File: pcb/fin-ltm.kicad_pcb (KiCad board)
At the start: 2 copper layers, 121 parts, among them J1 Connector, USB-TYPE-C-16P, Q1 MMBT3904, Q2 HL3415A, U1 ESP32-C3FH4, U2 RT9080, U3 SN74LV1T34DBV, X1 40MHz, 15pF

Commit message: server updates and battling with kicad
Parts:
- removed D11, D12, D13, D14, D15, D16, D17, D18, D19, D20, D21, D22, D23, D24, D25, D26, D27, D28, D29, D30, D31, D32, D33, D34, D35, D36, D37, D38, D39, D40, D41, D42, D43, D44, D45, D46, D47, D48, D49, D50, D51, D52, D53, D54, D55, D56, D57, D58, D59, D60, D61, D62, D63, D64, D65: WS2812B, PCM_JLCPCB:LED-SMD_4P-L1.6-W1.5_XL-1615RGBC-WS2812B
- added D101: WS2812B, PCM_JLCPCB:LED-SMD_4P-L1.6-W1.5_XL-1615RGBC-WS2812B, F.Cu at (66.6, 17.8)
- added D102: WS2812B, PCM_JLCPCB:LED-SMD_4P-L1.6-W1.5_XL-1615RGBC-WS2812B, F.Cu at (66.6, 20.4)
- added D103: WS2812B, PCM_JLCPCB:LED-SMD_4P-L1.6-W1.5_XL-1615RGBC-WS2812B, F.Cu at (66.6, 23.1)
- added D104: WS2812B, PCM_JLCPCB:LED-SMD_4P-L1.6-W1.5_XL-1615RGBC-WS2812B, F.Cu at (66.6, 25.7)
- added D105: WS2812B, PCM_JLCPCB:LED-SMD_4P-L1.6-W1.5_XL-1615RGBC-WS2812B, F.Cu at (66.6, 28.4)
- added D106: WS2812B, PCM_JLCPCB:LED-SMD_4P-L1.6-W1.5_XL-1615RGBC-WS2812B, F.Cu at (66.6, 31.0)
- added D107: WS2812B, PCM_JLCPCB:LED-SMD_4P-L1.6-W1.5_XL-1615RGBC-WS2812B, F.Cu at (66.6, 33.6)
- added D108: WS2812B, PCM_JLCPCB:LED-SMD_4P-L1.6-W1.5_XL-1615RGBC-WS2812B, F.Cu at (66.6, 36.3)
- added D109: WS2812B, PCM_JLCPCB:LED-SMD_4P-L1.6-W1.5_XL-1615RGBC-WS2812B, F.Cu at (66.6, 39.0)
- added D110: WS2812B, PCM_JLCPCB:LED-SMD_4P-L1.6-W1.5_XL-1615RGBC-WS2812B, F.Cu at (66.6, 41.6)
- added D111: WS2812B, PCM_JLCPCB:LED-SMD_4P-L1.6-W1.5_XL-1615RGBC-WS2812B, F.Cu at (66.6, 44.2)
- added D112: WS2812B, PCM_JLCPCB:LED-SMD_4P-L1.6-W1.5_XL-1615RGBC-WS2812B, F.Cu at (66.6, 46.9)
- added D113: WS2812B, PCM_JLCPCB:LED-SMD_4P-L1.6-W1.5_XL-1615RGBC-WS2812B, F.Cu at (66.6, 49.5)
- added D114: WS2812B, PCM_JLCPCB:LED-SMD_4P-L1.6-W1.5_XL-1615RGBC-WS2812B, F.Cu at (70.0, 17.8)
- added D115: WS2812B, PCM_JLCPCB:LED-SMD_4P-L1.6-W1.5_XL-1615RGBC-WS2812B, F.Cu at (70.0, 20.4)
- added D116: WS2812B, PCM_JLCPCB:LED-SMD_4P-L1.6-W1.5_XL-1615RGBC-WS2812B, F.Cu at (70.0, 23.1)
- added D117: WS2812B, PCM_JLCPCB:LED-SMD_4P-L1.6-W1.5_XL-1615RGBC-WS2812B, F.Cu at (70.0, 25.7)
- added D118: WS2812B, PCM_JLCPCB:LED-SMD_4P-L1.6-W1.5_XL-1615RGBC-WS2812B, F.Cu at (70.0, 28.4)
- added D119: WS2812B, PCM_JLCPCB:LED-SMD_4P-L1.6-W1.5_XL-1615RGBC-WS2812B, F.Cu at (70.0, 31.0)
- added D120: WS2812B, PCM_JLCPCB:LED-SMD_4P-L1.6-W1.5_XL-1615RGBC-WS2812B, F.Cu at (70.0, 33.6)
- added D121: WS2812B, PCM_JLCPCB:LED-SMD_4P-L1.6-W1.5_XL-1615RGBC-WS2812B, F.Cu at (70.0, 36.3)
- added D122: WS2812B, PCM_JLCPCB:LED-SMD_4P-L1.6-W1.5_XL-1615RGBC-WS2812B, F.Cu at (70.0, 39.0)
- added D123: WS2812B, PCM_JLCPCB:LED-SMD_4P-L1.6-W1.5_XL-1615RGBC-WS2812B, F.Cu at (70.0, 41.6)
- added D124: WS2812B, PCM_JLCPCB:LED-SMD_4P-L1.6-W1.5_XL-1615RGBC-WS2812B, F.Cu at (70.0, 44.2)
- added D125: WS2812B, PCM_JLCPCB:LED-SMD_4P-L1.6-W1.5_XL-1615RGBC-WS2812B, F.Cu at (70.0, 46.9)
- added D126: WS2812B, PCM_JLCPCB:LED-SMD_4P-L1.6-W1.5_XL-1615RGBC-WS2812B, F.Cu at (70.0, 49.5)
- added D127: WS2812B, PCM_JLCPCB:LED-SMD_4P-L1.6-W1.5_XL-1615RGBC-WS2812B, F.Cu at (73.5, 17.8)
- added D128: WS2812B, PCM_JLCPCB:LED-SMD_4P-L1.6-W1.5_XL-1615RGBC-WS2812B, F.Cu at (73.5, 20.4)
- added D129: WS2812B, PCM_JLCPCB:LED-SMD_4P-L1.6-W1.5_XL-1615RGBC-WS2812B, F.Cu at (73.5, 23.1)
- added D130: WS2812B, PCM_JLCPCB:LED-SMD_4P-L1.6-W1.5_XL-1615RGBC-WS2812B, F.Cu at (73.5, 25.7)
- added D131: WS2812B, PCM_JLCPCB:LED-SMD_4P-L1.6-W1.5_XL-1615RGBC-WS2812B, F.Cu at (73.5, 28.4)
- added D132: WS2812B, PCM_JLCPCB:LED-SMD_4P-L1.6-W1.5_XL-1615RGBC-WS2812B, F.Cu at (73.5, 31.0)
- added D133: WS2812B, PCM_JLCPCB:LED-SMD_4P-L1.6-W1.5_XL-1615RGBC-WS2812B, F.Cu at (73.5, 33.6)
- added D134: WS2812B, PCM_JLCPCB:LED-SMD_4P-L1.6-W1.5_XL-1615RGBC-WS2812B, F.Cu at (73.5, 36.3)
- added D135: WS2812B, PCM_JLCPCB:LED-SMD_4P-L1.6-W1.5_XL-1615RGBC-WS2812B, F.Cu at (73.5, 39.0)
- added D136: WS2812B, PCM_JLCPCB:LED-SMD_4P-L1.6-W1.5_XL-1615RGBC-WS2812B, F.Cu at (73.5, 41.6)
- added D137: WS2812B, PCM_JLCPCB:LED-SMD_4P-L1.6-W1.5_XL-1615RGBC-WS2812B, F.Cu at (73.5, 44.2)
- added D138: WS2812B, PCM_JLCPCB:LED-SMD_4P-L1.6-W1.5_XL-1615RGBC-WS2812B, F.Cu at (73.5, 46.9)
- added D139: WS2812B, PCM_JLCPCB:LED-SMD_4P-L1.6-W1.5_XL-1615RGBC-WS2812B, F.Cu at (73.5, 49.5)
- added D140: WS2812B, PCM_JLCPCB:LED-SMD_4P-L1.6-W1.5_XL-1615RGBC-WS2812B, F.Cu at (77.0, 17.8)
- added D141: WS2812B, PCM_JLCPCB:LED-SMD_4P-L1.6-W1.5_XL-1615RGBC-WS2812B, F.Cu at (77.0, 20.4)
- added D142: WS2812B, PCM_JLCPCB:LED-SMD_4P-L1.6-W1.5_XL-1615RGBC-WS2812B, F.Cu at (77.0, 23.1)
- added D143: WS2812B, PCM_JLCPCB:LED-SMD_4P-L1.6-W1.5_XL-1615RGBC-WS2812B, F.Cu at (77.0, 25.7)
- added D144: WS2812B, PCM_JLCPCB:LED-SMD_4P-L1.6-W1.5_XL-1615RGBC-WS2812B, F.Cu at (77.0, 28.4)
- added D145: WS2812B, PCM_JLCPCB:LED-SMD_4P-L1.6-W1.5_XL-1615RGBC-WS2812B, F.Cu at (77.0, 31.0)
- added D146: WS2812B, PCM_JLCPCB:LED-SMD_4P-L1.6-W1.5_XL-1615RGBC-WS2812B, F.Cu at (77.0, 33.6)
- added D147: WS2812B, PCM_JLCPCB:LED-SMD_4P-L1.6-W1.5_XL-1615RGBC-WS2812B, F.Cu at (77.0, 36.3)
- added D148: WS2812B, PCM_JLCPCB:LED-SMD_4P-L1.6-W1.5_XL-1615RGBC-WS2812B, F.Cu at (77.0, 39.0)
- added D149: WS2812B, PCM_JLCPCB:LED-SMD_4P-L1.6-W1.5_XL-1615RGBC-WS2812B, F.Cu at (77.0, 41.6)
- added D150: WS2812B, PCM_JLCPCB:LED-SMD_4P-L1.6-W1.5_XL-1615RGBC-WS2812B, F.Cu at (77.0, 44.2)
- added D151: WS2812B, PCM_JLCPCB:LED-SMD_4P-L1.6-W1.5_XL-1615RGBC-WS2812B, F.Cu at (77.0, 46.9)
- added D152: WS2812B, PCM_JLCPCB:LED-SMD_4P-L1.6-W1.5_XL-1615RGBC-WS2812B, F.Cu at (77.0, 49.5)
- added D153: WS2812B, PCM_JLCPCB:LED-SMD_4P-L1.6-W1.5_XL-1615RGBC-WS2812B, F.Cu at (80.4, 17.8)
- added D154: WS2812B, PCM_JLCPCB:LED-SMD_4P-L1.6-W1.5_XL-1615RGBC-WS2812B, F.Cu at (80.4, 20.4)
- added D155: WS2812B, PCM_JLCPCB:LED-SMD_4P-L1.6-W1.5_XL-1615RGBC-WS2812B, F.Cu at (80.4, 23.1)
- added D156: WS2812B, PCM_JLCPCB:LED-SMD_4P-L1.6-W1.5_XL-1615RGBC-WS2812B, F.Cu at (80.4, 25.7)
- added D157: WS2812B, PCM_JLCPCB:LED-SMD_4P-L1.6-W1.5_XL-1615RGBC-WS2812B, F.Cu at (80.4, 28.4)
- added D158: WS2812B, PCM_JLCPCB:LED-SMD_4P-L1.6-W1.5_XL-1615RGBC-WS2812B, F.Cu at (80.4, 31.0)
- added D159: WS2812B, PCM_JLCPCB:LED-SMD_4P-L1.6-W1.5_XL-1615RGBC-WS2812B, F.Cu at (80.4, 33.6)
- added D160: WS2812B, PCM_JLCPCB:LED-SMD_4P-L1.6-W1.5_XL-1615RGBC-WS2812B, F.Cu at (80.4, 36.3)
- added D161: WS2812B, PCM_JLCPCB:LED-SMD_4P-L1.6-W1.5_XL-1615RGBC-WS2812B, F.Cu at (80.4, 39.0)
- added D162: WS2812B, PCM_JLCPCB:LED-SMD_4P-L1.6-W1.5_XL-1615RGBC-WS2812B, F.Cu at (80.4, 41.6)
- added D163: WS2812B, PCM_JLCPCB:LED-SMD_4P-L1.6-W1.5_XL-1615RGBC-WS2812B, F.Cu at (80.4, 44.2)
- added D164: WS2812B, PCM_JLCPCB:LED-SMD_4P-L1.6-W1.5_XL-1615RGBC-WS2812B, F.Cu at (80.4, 46.9)
- added D165: WS2812B, PCM_JLCPCB:LED-SMD_4P-L1.6-W1.5_XL-1615RGBC-WS2812B, F.Cu at (80.4, 49.5)
- added D166: WS2812B, PCM_JLCPCB:LED-SMD_4P-L1.6-W1.5_XL-1615RGBC-WS2812B, F.Cu at (83.8, 17.8)
- added D167: WS2812B, PCM_JLCPCB:LED-SMD_4P-L1.6-W1.5_XL-1615RGBC-WS2812B, F.Cu at (83.8, 20.4)
- added D168: WS2812B, PCM_JLCPCB:LED-SMD_4P-L1.6-W1.5_XL-1615RGBC-WS2812B, F.Cu at (83.8, 23.1)
- added D169: WS2812B, PCM_JLCPCB:LED-SMD_4P-L1.6-W1.5_XL-1615RGBC-WS2812B, F.Cu at (83.8, 25.7)
- added D170: WS2812B, PCM_JLCPCB:LED-SMD_4P-L1.6-W1.5_XL-1615RGBC-WS2812B, F.Cu at (83.8, 28.4)
- added D171: WS2812B, PCM_JLCPCB:LED-SMD_4P-L1.6-W1.5_XL-1615RGBC-WS2812B, F.Cu at (83.8, 31.0)
- added D172: WS2812B, PCM_JLCPCB:LED-SMD_4P-L1.6-W1.5_XL-1615RGBC-WS2812B, F.Cu at (83.8, 33.6)
- added D173: WS2812B, PCM_JLCPCB:LED-SMD_4P-L1.6-W1.5_XL-1615RGBC-WS2812B, F.Cu at (83.8, 36.3)
- added D174: WS2812B, PCM_JLCPCB:LED-SMD_4P-L1.6-W1.5_XL-1615RGBC-WS2812B, F.Cu at (83.8, 39.0)
- added D175: WS2812B, PCM_JLCPCB:LED-SMD_4P-L1.6-W1.5_XL-1615RGBC-WS2812B, F.Cu at (83.8, 41.6)
- added D176: WS2812B, PCM_JLCPCB:LED-SMD_4P-L1.6-W1.5_XL-1615RGBC-WS2812B, F.Cu at (83.8, 44.2)
- added D177: WS2812B, PCM_JLCPCB:LED-SMD_4P-L1.6-W1.5_XL-1615RGBC-WS2812B, F.Cu at (83.8, 46.9)
- added D178: WS2812B, PCM_JLCPCB:LED-SMD_4P-L1.6-W1.5_XL-1615RGBC-WS2812B, F.Cu at (83.8, 49.5)
- added D179: WS2812B, PCM_JLCPCB:LED-SMD_4P-L1.6-W1.5_XL-1615RGBC-WS2812B, F.Cu at (87.3, 17.8)
- added D180: WS2812B, PCM_JLCPCB:LED-SMD_4P-L1.6-W1.5_XL-1615RGBC-WS2812B, F.Cu at (87.3, 20.4)
- added D181: WS2812B, PCM_JLCPCB:LED-SMD_4P-L1.6-W1.5_XL-1615RGBC-WS2812B, F.Cu at (87.3, 23.1)
- added D182: WS2812B, PCM_JLCPCB:LED-SMD_4P-L1.6-W1.5_XL-1615RGBC-WS2812B, F.Cu at (87.3, 25.7)
- added D183: WS2812B, PCM_JLCPCB:LED-SMD_4P-L1.6-W1.5_XL-1615RGBC-WS2812B, F.Cu at (87.3, 28.4)
- added D184: WS2812B, PCM_JLCPCB:LED-SMD_4P-L1.6-W1.5_XL-1615RGBC-WS2812B, F.Cu at (87.3, 31.0)
- added D185: WS2812B, PCM_JLCPCB:LED-SMD_4P-L1.6-W1.5_XL-1615RGBC-WS2812B, F.Cu at (87.3, 33.6)
- added D186: WS2812B, PCM_JLCPCB:LED-SMD_4P-L1.6-W1.5_XL-1615RGBC-WS2812B, F.Cu at (87.3, 36.3)
- added D187: WS2812B, PCM_JLCPCB:LED-SMD_4P-L1.6-W1.5_XL-1615RGBC-WS2812B, F.Cu at (87.3, 39.0)
- added D188: WS2812B, PCM_JLCPCB:LED-SMD_4P-L1.6-W1.5_XL-1615RGBC-WS2812B, F.Cu at (87.3, 41.6)
- added D189: WS2812B, PCM_JLCPCB:LED-SMD_4P-L1.6-W1.5_XL-1615RGBC-WS2812B, F.Cu at (87.3, 44.2)
- added D190: WS2812B, PCM_JLCPCB:LED-SMD_4P-L1.6-W1.5_XL-1615RGBC-WS2812B, F.Cu at (87.3, 46.9)
- added D191: WS2812B, PCM_JLCPCB:LED-SMD_4P-L1.6-W1.5_XL-1615RGBC-WS2812B, F.Cu at (87.3, 49.5)
- added D192: WS2812B, PCM_JLCPCB:LED-SMD_4P-L1.6-W1.5_XL-1615RGBC-WS2812B, F.Cu at (90.8, 17.8)
- added D193: WS2812B, PCM_JLCPCB:LED-SMD_4P-L1.6-W1.5_XL-1615RGBC-WS2812B, F.Cu at (90.8, 20.4)
- added D194: WS2812B, PCM_JLCPCB:LED-SMD_4P-L1.6-W1.5_XL-1615RGBC-WS2812B, F.Cu at (90.8, 23.1)
- added D195: WS2812B, PCM_JLCPCB:LED-SMD_4P-L1.6-W1.5_XL-1615RGBC-WS2812B, F.Cu at (90.8, 25.7)
- added D196: WS2812B, PCM_JLCPCB:LED-SMD_4P-L1.6-W1.5_XL-1615RGBC-WS2812B, F.Cu at (90.8, 28.4)
- added D197: WS2812B, PCM_JLCPCB:LED-SMD_4P-L1.6-W1.5_XL-1615RGBC-WS2812B, F.Cu at (90.8, 31.0)
- added D198: WS2812B, PCM_JLCPCB:LED-SMD_4P-L1.6-W1.5_XL-1615RGBC-WS2812B, F.Cu at (90.8, 33.6)
- added D199: WS2812B, PCM_JLCPCB:LED-SMD_4P-L1.6-W1.5_XL-1615RGBC-WS2812B, F.Cu at (90.8, 36.3)
- added D200: WS2812B, PCM_JLCPCB:LED-SMD_4P-L1.6-W1.5_XL-1615RGBC-WS2812B, F.Cu at (90.8, 39.0)
- moved J1 58.5 mm to (54.8, 29.1)
- moved F1 23.5 mm to (57.2, 46.6)
- moved X1 23.5 mm to (51.9, 47.1)
- moved D6 23.5 mm to (61.1, 45.8)
- moved Q1 20.6 mm to (33.0, 44.5)
- moved Q2 20.6 mm to (33.0, 49.1)
- moved U2 20.1 mm to (57.7, 37.3)
- moved U3 20.1 mm to (57.7, 41.9)
- moved U1 19.0 mm to (38.9, 45.6)
- moved C10 18.5 mm to (47.1, 51.5)
- moved C8 18.5 mm to (47.1, 45.4)
- moved C9 18.5 mm to (47.1, 48.4)
- moved D10 18.5 mm to (47.1, 42.3)
- moved D7 18.5 mm to (47.1, 33.1)
- moved D8 18.5 mm to (47.1, 36.2)
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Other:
- board text removed: "REF**"

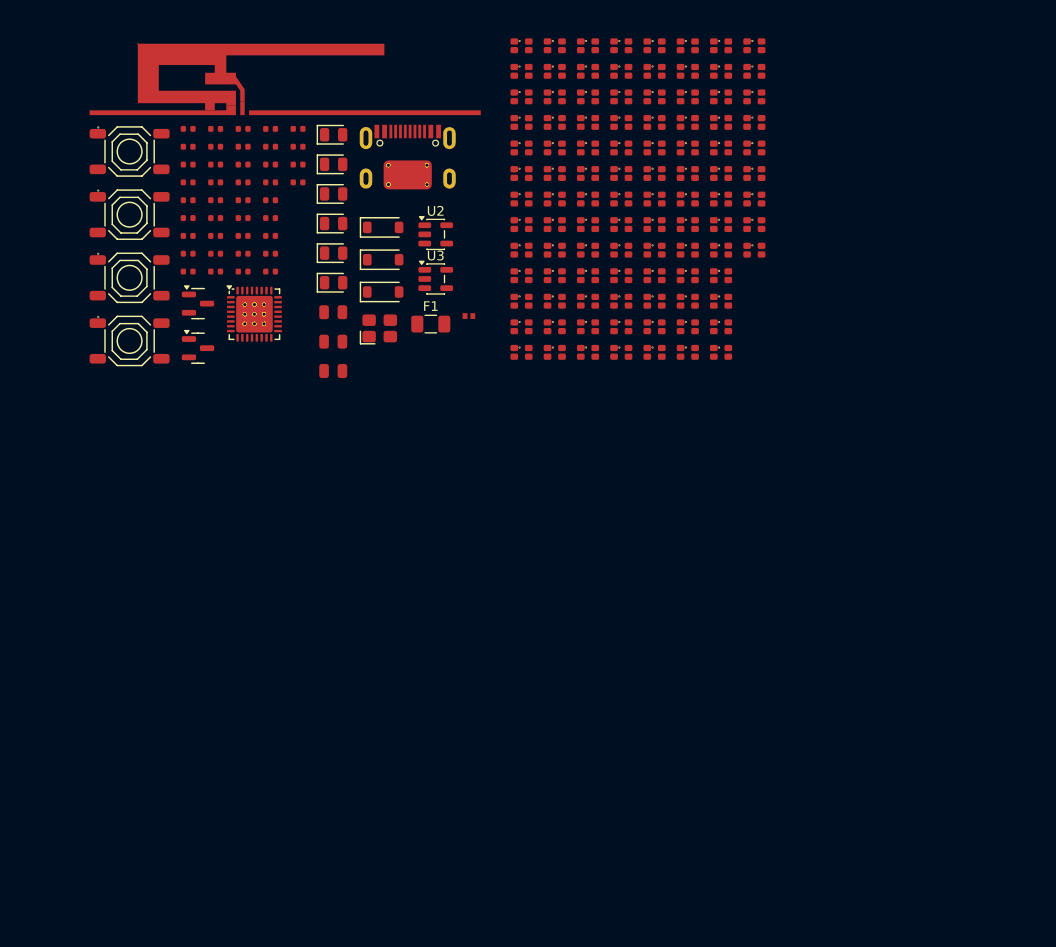
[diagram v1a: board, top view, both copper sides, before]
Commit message: pcb designed antenna
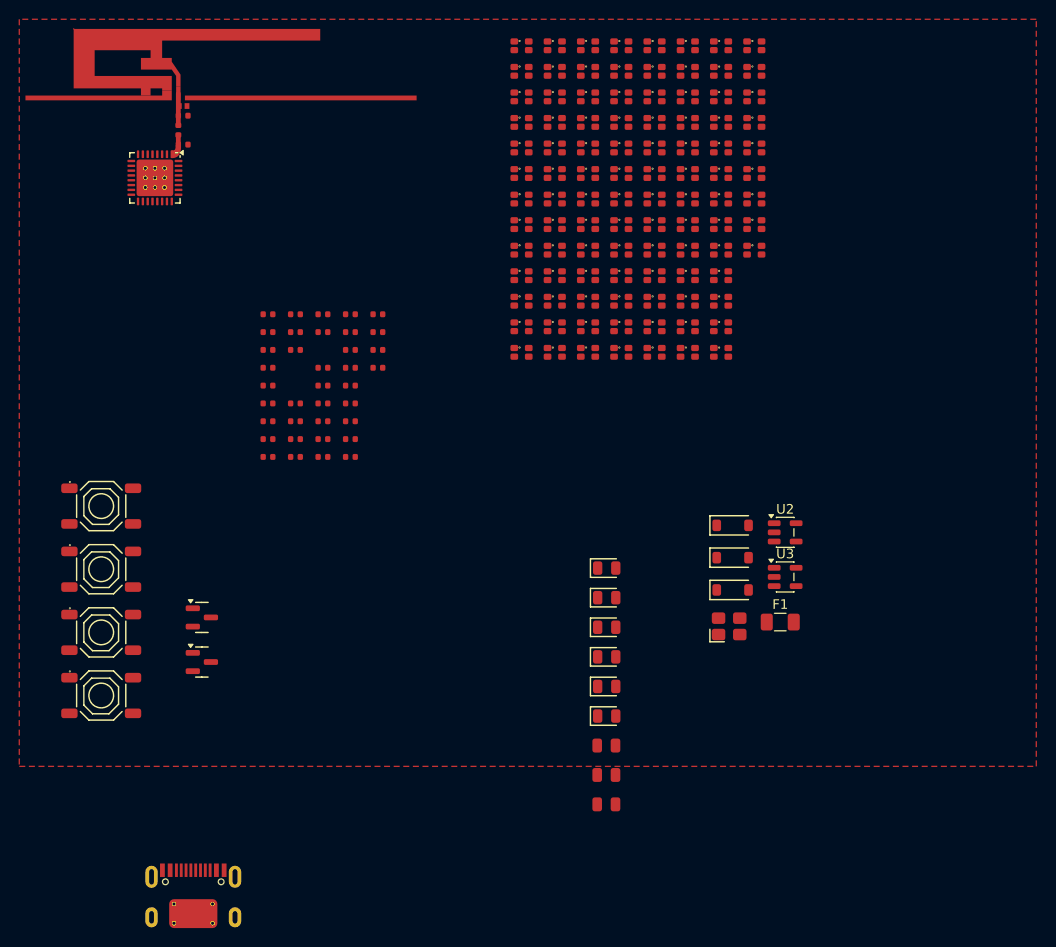
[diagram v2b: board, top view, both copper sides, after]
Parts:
- moved J1 79.8 mm to (32.5, 105.8)
- moved C8 53.1 mm to (75.4, 90.3)
- moved C9 53.1 mm to (75.4, 93.4)
- moved C10 53.1 mm to (75.4, 96.4)
- moved D7 53.1 mm to (75.4, 78.1)
- moved D9 53.1 mm to (75.4, 84.2)
- moved D1 53.1 mm to (75.4, 71.9)
- moved D10 53.1 mm to (75.4, 87.3)
- moved D5 53.1 mm to (75.4, 75.0)
- moved D8 53.1 mm to (75.4, 81.1)
- moved D4 47.6 mm to (88.5, 74.2)
- moved F1 47.6 mm to (93.4, 77.5)
- moved D2 47.6 mm to (88.5, 67.5)
- moved D3 47.6 mm to (88.5, 70.8)
- moved U2 47.6 mm to (94.0, 68.2)
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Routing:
- net Net-(AE1-A): track 0.00 -> 3.30 mm
- net /Antenna: track 0.00 -> 1.00 mm
- added copper zone on F.Cu, net GND
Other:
- rule pad_to_mask_clearance: 0 -> 0.05

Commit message: pcb update and planning in svg
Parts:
- moved U3 83.6 mm to (20.6, 32.8), turned to 180 degrees
- moved X1 70.1 mm to (35.2, 32.0), turned to -90 degrees
- moved R9 36.2 mm to (16.9, 32.2), turned to 90 degrees
- moved R19 35.1 mm to (26.5, 26.8), turned to -90 degrees
- moved R8 34.5 mm to (17.9, 32.2), turned to 90 degrees
- moved R10 32.4 mm to (27.5, 26.8), turned to -90 degrees
- moved R18 32.4 mm to (28.5, 26.8), turned to -90 degrees
- moved C7 31.8 mm to (29.5, 26.8), turned to -90 degrees
- moved C6 29.6 mm to (24.2, 30.0)
- moved C11 26.2 mm to (27.8, 35.5), turned to -90 degrees
- moved C4 22.8 mm to (32.5, 29.8), turned to 180 degrees
- moved C5 22.1 mm to (26.8, 35.5), turned to 90 degrees
- moved L1 21.5 mm to (32.5, 30.8), turned to 180 degrees
- moved C15 19.8 mm to (33.0, 32.2), turned to 90 degrees
- moved C14 19.8 mm to (34.8, 29.5)
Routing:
- net /Leds/LED_DATA_5V: track 0.00 -> 27.1 mm, vias 0 -> 1
- net +3V3: track 0.00 -> 23.7 mm, vias 0 -> 4
- net Net-(U1-XTAL_N): track 0.00 -> 5.87 mm
- net /LED_DATA_3V3: track 0.00 -> 3.42 mm
- net Net-(C14-Pad1): track 0.00 -> 2.71 mm
- net /MODE_BUTTON: track 0.00 -> 2.03 mm
- net /POWER_BUTTON: track 0.00 -> 1.88 mm
- net /Reset: track 0.00 -> 1.82 mm
- net Net-(U3-Y): track 0.00 -> 1.63 mm
- net Net-(U1-(OUTPUT)_VDD_SPI): track 0.00 -> 1.28 mm
- net Net-(U1-XTAL_P): track 0.00 -> 1.00 mm
- net GND: vias 0 -> 20
- added copper zone on B.Cu, net GND
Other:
- board text added: "To led chain"

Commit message: more pcb routing
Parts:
- added J2: Test Connector, Library:Test_connector, F.Cu at (24.5, 52.3)
- moved S1 55.4 mm to (76.5, 79.9)
- moved S2 55.4 mm to (76.5, 86.5)
- moved S3 55.4 mm to (76.5, 93.0)
- moved S4 55.4 mm to (76.5, 99.5)
- moved J1 24.6 mm to (23.2, 83.0), turned to -90 degrees
- moved R11 18.5 mm to (43.8, 35.2), turned to 90 degrees
- moved C15 15.2 mm to (47.8, 36.0)
- moved U1 10.7 mm to (39.1, 33.7)
- moved C1 10.7 mm to (50.8, 47.9)
- moved C10 10.7 mm to (85.9, 98.7)
- moved C11 10.7 mm to (38.2, 37.8)
- moved C12 10.7 mm to (50.8, 62.6)
- moved C13 10.7 mm to (53.6, 47.9)
- moved C14 10.7 mm to (45.2, 31.8)
- moved C16 10.7 mm to (42.0, 27.2)
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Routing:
- net /USB_D+: track 0.00 -> 65.4 mm, vias 0 -> 2
- net /USB_D-: track 0.00 -> 64.4 mm, vias 0 -> 2
- net /Reset: track 1.82 -> 32.2 mm, vias 0 -> 1
- net /MCU_RX: track 0.00 -> 29.6 mm, vias 0 -> 1
- net /MCU_TX: track 0.00 -> 29.1 mm, vias 0 -> 1
- net /Leds/LED_DATA_5V: track 27.1 -> 6.18 mm
- net Net-(U1-U0TXD): track 0.00 -> 2.56 mm
- net Net-(U1-XTAL_N): track 5.87 -> 7.08 mm
- net /LED_DATA_3V3: track 3.42 -> 4.56 mm
- net GND: vias 20 -> 18
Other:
- board outline added: 112.5 x 77.3 mm

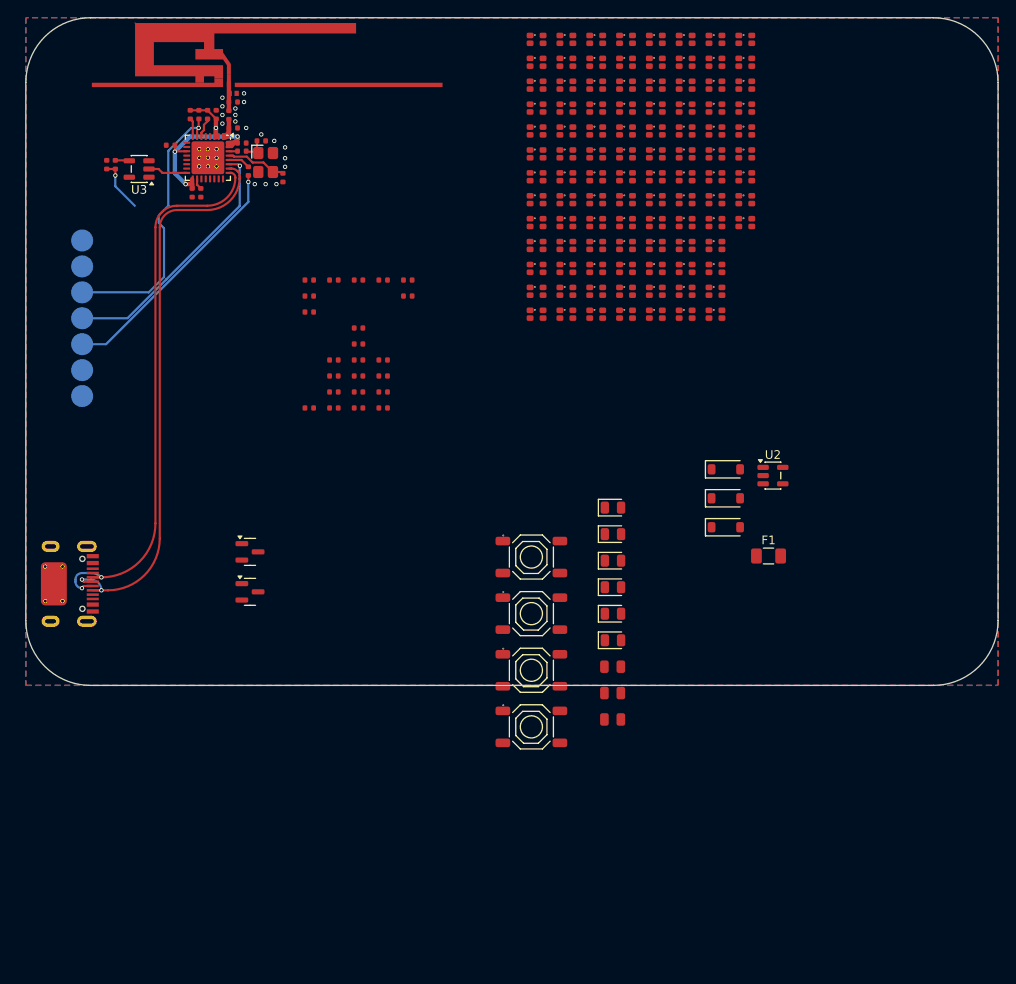
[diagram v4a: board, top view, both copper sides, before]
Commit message: even more pcb routing
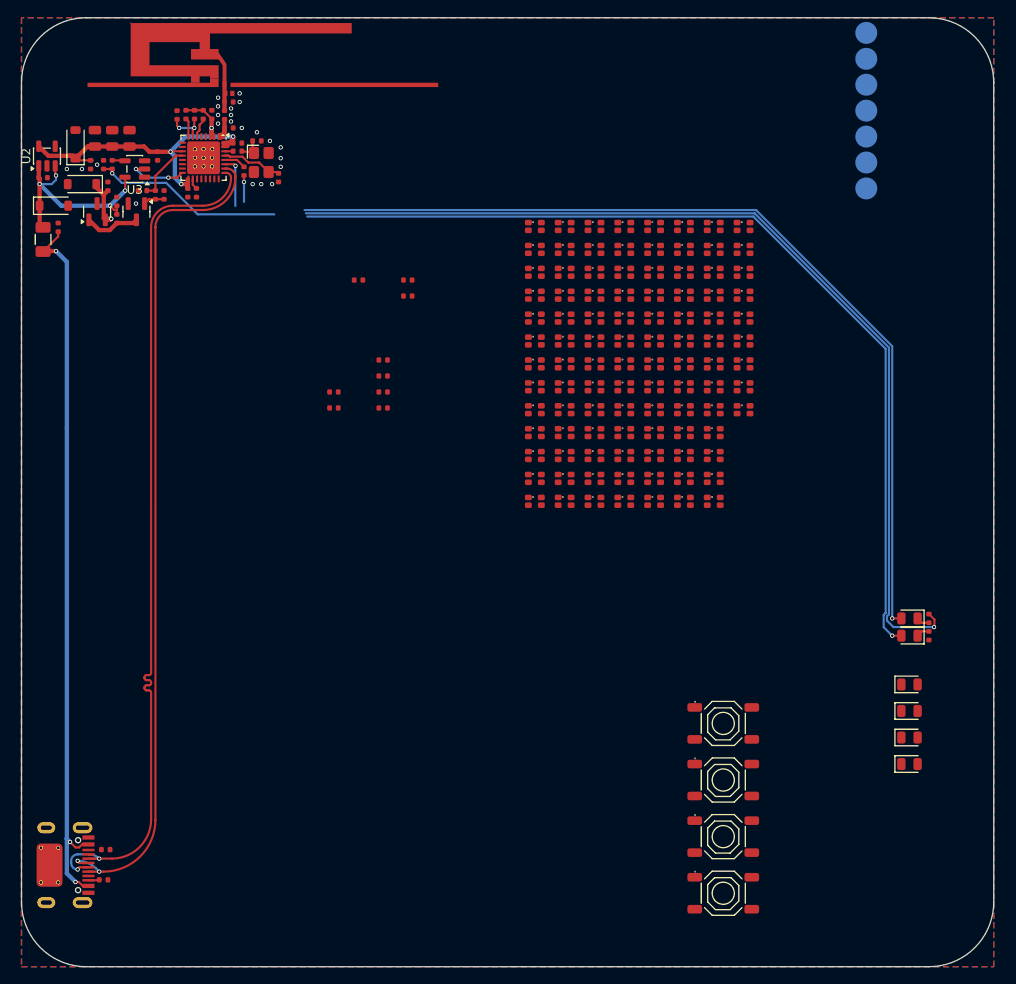
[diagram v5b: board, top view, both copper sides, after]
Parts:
- moved J2 93.9 mm to (115.2, 28.2)
- moved U2 91.8 mm to (20.4, 33.5), turned to 90 degrees
- moved F1 91.6 mm to (20.0, 43.1), turned to 90 degrees
- moved C10 87.4 mm to (30.0, 31.4), turned to 90 degrees
- moved C9 86.4 mm to (28.0, 31.4), turned to 90 degrees
- moved D3 85.7 mm to (23.8, 32.1), turned to 90 degrees
- moved C8 85.6 mm to (26.0, 31.4), turned to 90 degrees
- moved D4 84.4 mm to (24.5, 36.8), turned to 180 degrees
- moved D2 83.5 mm to (21.2, 39.2)
- moved R7 75.4 mm to (122.5, 89.0), turned to -90 degrees
- moved R3 72.5 mm to (122.5, 87.0), turned to -90 degrees
- moved R1 70.3 mm to (27.0, 117.2), turned to 180 degrees
- moved R2 65.4 mm to (27.2, 113.8)
- moved Q2 47.4 mm to (26.2, 39.9), turned to 90 degrees
- moved Q1 41.5 mm to (30.8, 39.9), turned to -90 degrees
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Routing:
- net Net-(C1-Pad2): track 0.00 -> 190.3 mm, vias 0 -> 4
- net VBUS: track 0.00 -> 139.7 mm, vias 0 -> 5
- net +3V3: track 23.7 -> 150.8 mm, vias 4 -> 5
- net /USB_D-: track 64.4 -> 100.3 mm
- net /USB_D+: track 65.4 -> 97.9 mm
- net /Reset: track 32.2 -> 4.98 mm, vias 1 -> 2
- net /MCU_TX: track 29.1 -> 3.06 mm
- net /MCU_RX: track 29.6 -> 5.98 mm
- net /Leds/LED_DATA_5V: track 6.18 -> 22.2 mm
- net /LED_POWER_CTRL: track 0.00 -> 6.79 mm
- net +5V: track 0.00 -> 6.53 mm, vias 0 -> 1
- net Net-(Q1-C): track 0.00 -> 6.49 mm
- net Net-(Q1-B): track 0.00 -> 2.46 mm
- net /LED_DATA_3V3: track 4.56 -> 7.00 mm, vias 0 -> 2
- net Net-(D5-Pad1): track 0.00 -> 1.52 mm
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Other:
- board size 112.5 x 77.3 mm -> 112.5 x 109.8 mm

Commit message: pcb
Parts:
- moved R14 74.6 mm to (122.5, 100.5), turned to -90 degrees
- moved R12 73.5 mm to (122.5, 94.8), turned to -90 degrees
- moved R15 72.6 mm to (122.5, 98.5), turned to 90 degrees
- moved R13 71.6 mm to (122.5, 92.8), turned to 90 degrees
- moved C22 43.5 mm to (91.5, 22.0)
- moved C21 37.7 mm to (28.5, 34.5), turned to 90 degrees
- moved C20 34.6 mm to (28.5, 37.0), turned to -90 degrees
- moved R16 28.9 mm to (35.0, 38.0), turned to 90 degrees
- moved R17 28.7 mm to (36.0, 38.0), turned to 90 degrees
- moved D10 5.35 mm to (120.2, 98.5), turned to 180 degrees
- moved D112 5.12 mm to (75.2, 75.7)
- moved D151 5.12 mm to (85.6, 75.7)
- moved D164 5.12 mm to (89.0, 75.7)
- moved D177 5.12 mm to (92.5, 75.7)
- moved D125 5.12 mm to (78.7, 75.7)
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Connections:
- R18 pad 2: /MODE_BUTTON -> /DISPLAY_SCL
- R19 pad 2: /POWER_BUTTON -> /DISPLAY_SDA
- U1 pad 10: /SERVER_LED -> /WIFI_LED
- U1 pad 14: /BRIGHTNESS_UP_BUTTON -> /LED_DATA_3V3
- U1 pad 15: /BRIGHTNESS_DOWN_BUTTON -> /BRIGHTNESS_UP_BUTTON
- U1 pad 16: /LED_DATA_3V3 -> /BRIGHTNESS_DOWN_BUTTON
- U1 pad 9: /WIFI_LED -> /SERVER_LED
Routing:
- net /SERVER_LED: track 0.00 -> 149.7 mm, vias 0 -> 5
- net /WIFI_LED: track 0.00 -> 142.1 mm, vias 0 -> 5
- net +3V3: track 150.8 -> 189.3 mm, vias 5 -> 10
- net VBUS: track 139.7 -> 174.3 mm, vias 5 -> 6
- net Net-(C1-Pad2): track 190.3 -> 222.5 mm, vias 4 -> 6
- net /DISPLAY_SCL: track 0.00 -> 16.2 mm, vias 0 -> 1
- net /DISPLAY_SDA: track 0.00 -> 16.2 mm, vias 0 -> 1
- net /Leds/LED_DATA_5V: track 22.2 -> 35.2 mm, vias 1 -> 3
- net /Reset: track 4.98 -> 17.9 mm, vias 2 -> 1
- net GND: track 0.00 -> 12.4 mm, vias 22 -> 28
- net /POWER_BUTTON: track 2.16 -> 13.9 mm, vias 0 -> 1
- net /BRIGHTNESS_UP_BUTTON: track 0.00 -> 10.0 mm, vias 0 -> 1
- net /BRIGHTNESS_DOWN_BUTTON: track 0.00 -> 7.78 mm, vias 0 -> 1
- net /LED_POWER_CTRL: track 6.79 -> 10.9 mm, vias 0 -> 2
- net /LED_DATA_3V3: track 7.00 -> 4.54 mm, vias 2 -> 0
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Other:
- board text removed: "To led chain"
